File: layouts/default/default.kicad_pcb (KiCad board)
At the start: 2 copper layers, 39 x 17 mm, 21 parts

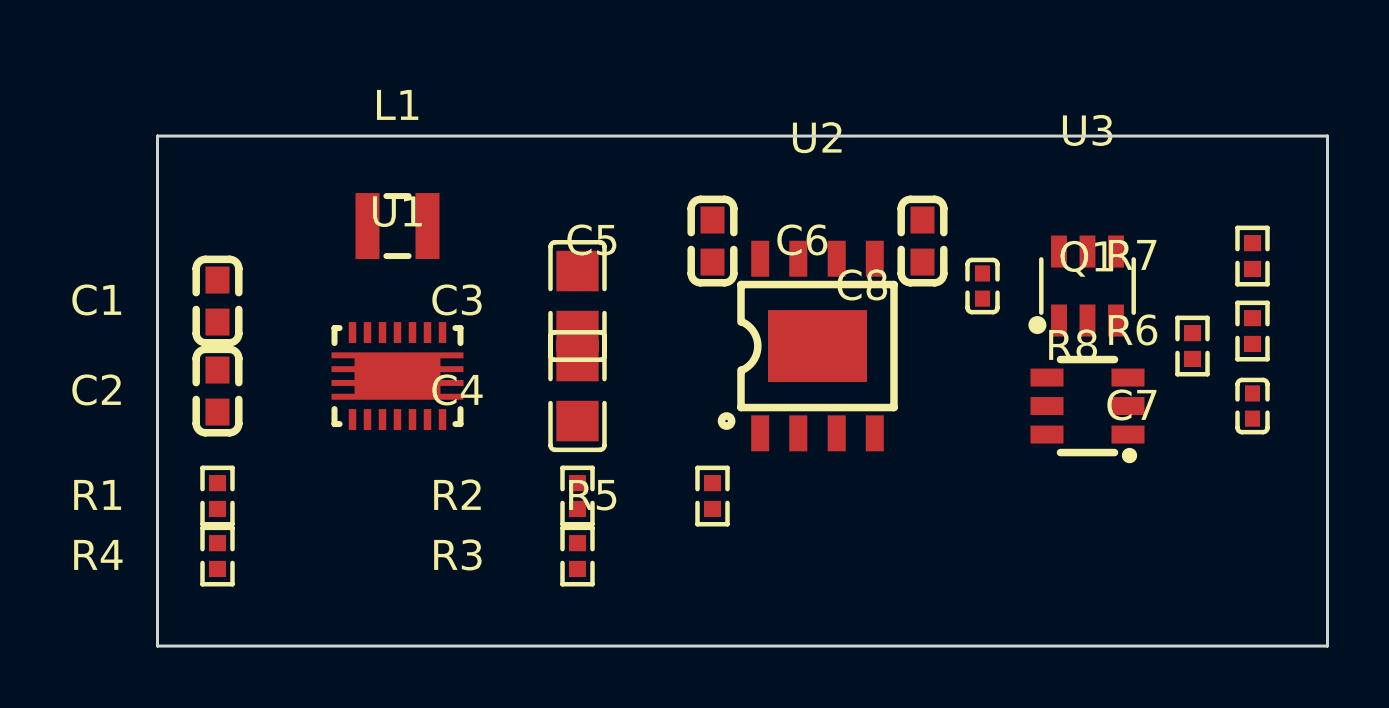
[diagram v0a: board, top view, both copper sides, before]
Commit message: Simplify: remove battery protection, add AO3401A P-MOSFET power switch for Pi (35x15mm, 19 components)
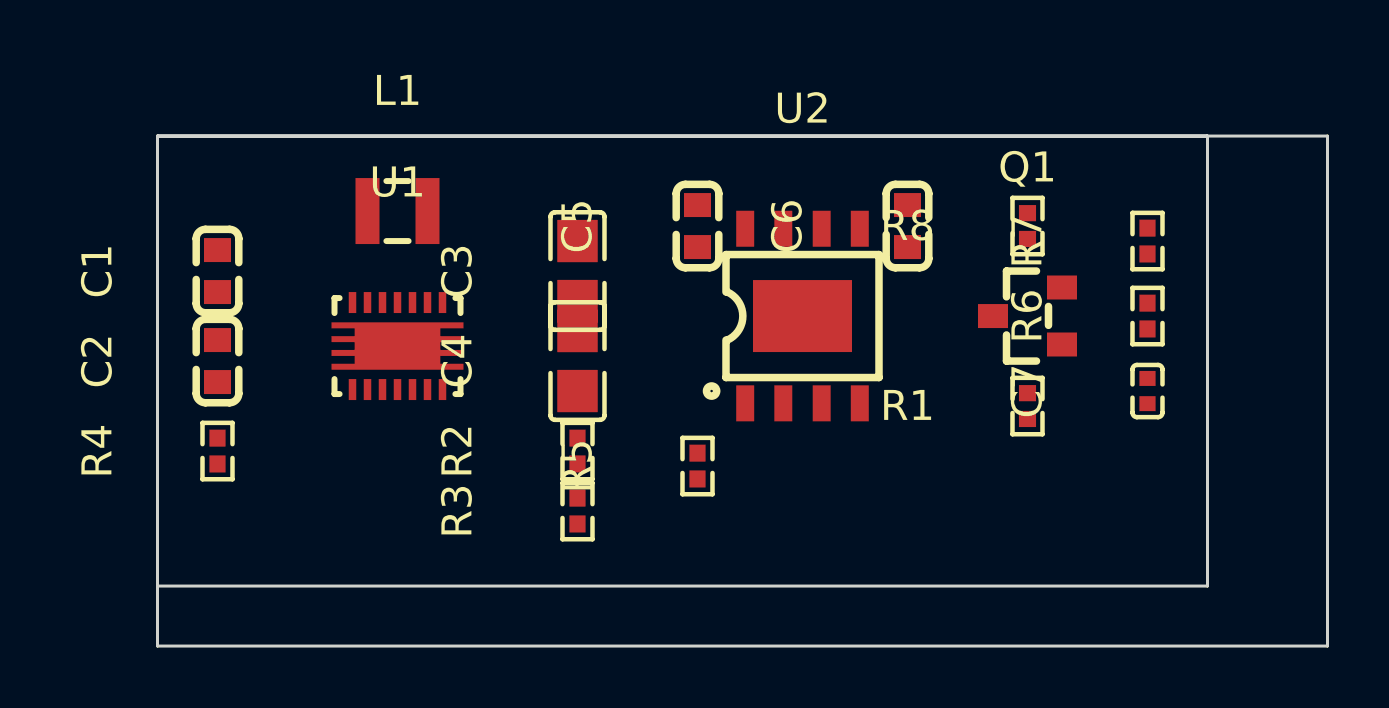
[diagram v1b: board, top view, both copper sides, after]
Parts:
- removed C8: 0F, Samsung_Electro_Mechanics_CL05B104KO5NNNC:C0402
- removed U3: , PUOLOP_DW01A:SOT-23-6_L2.9-W1.6-P0.95-LS2.8-BL
- Q1: footprint Fortune_Semicon_FS8205:SOT-23-6_L2.9-W1.6-P0.95-LS2.8-BR -> Alpha___Omega_Semicon_AO3401A:SOT-23_L2.9-W1.3-P1.90-LS2.4-BR
- R1: value 100000Ω -> 10000Ω; footprint UNI_ROYAL_0402WGF1003TCE:R0402 -> UNI_ROYAL_0402WGF1002TCE:R0402
- R8: value 100Ω -> 100000Ω; footprint UNI_ROYAL_0402WGF1000TCE:R0402 -> UNI_ROYAL_0402WGF1003TCE:R0402
- moved R1 27.2 mm to (128.0, 89.0)
- moved R8 6.80 mm to (128.0, 83.0)
- moved Q1 3.61 mm to (128.0, 86.0)
- moved C7 3.54 mm to (132.0, 88.5)
- moved R6 3.54 mm to (132.0, 86.0)
- moved R7 3.54 mm to (132.0, 83.5)
- moved R4 3.50 mm to (101.0, 90.5)
- moved R2 1.50 mm to (113.0, 90.5)
- moved R3 1.50 mm to (113.0, 92.5)
- moved R5 1.12 mm to (117.0, 91.0)
- moved U2 1.12 mm to (120.5, 86.0)
- moved C1 1.00 mm to (101.0, 84.5)
- moved C2 1.00 mm to (101.0, 87.5)
- moved C3 1.00 mm to (113.0, 84.5)
- moved C4 1.00 mm to (113.0, 87.5)
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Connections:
- C1 pad 2: c_vout2-power-lv -> lv
- C2 pad 2: c_vout2-power-lv -> lv
- C3 pad 2: c_vout2-power-lv -> lv
- C4 pad 2: c_vout2-power-lv -> lv
- C5 pad 1: hv -> c_bat-power-hv
- C5 pad 2: c_vout2-power-lv -> lv
- C6 pad 2: c_vout2-power-lv -> lv
- C7 pad 2: c_vout2-power-lv -> lv
- Q1 pad 1: c_vout2-power-lv -> pi_en
- Q1 pad 2: 2 -> c_bat-power-hv
- Q1 pad 3: lv -> hv
- R1 pad 2: c_vout2-power-lv -> lv
- R2 pad 2: c_vout2-power-lv -> lv
- R4 pad 2: c_vout2-power-lv -> lv
- R5 pad 2: c_vout2-power-lv -> lv
- R6 pad 2: c_vout2-power-lv -> lv
- R7 pad 1: hv -> c_bat-power-hv
- R8 pad 1: lv -> c_bat-power-hv
- R8 pad 2: VM -> pi_en
- U1 pad 12: pi_en -> hv
- U1 pad 15: c_vout2-power-lv -> lv
- U1 pad 2: c_vout2-power-lv -> lv
- U2 pad 1: c_vout2-power-lv -> lv
- U2 pad 3: c_vout2-power-lv -> lv
- U2 pad 5: hv -> c_bat-power-hv
- U2 pad 9: c_vout2-power-lv -> lv
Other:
- outline, holes or cut-outs redrawn

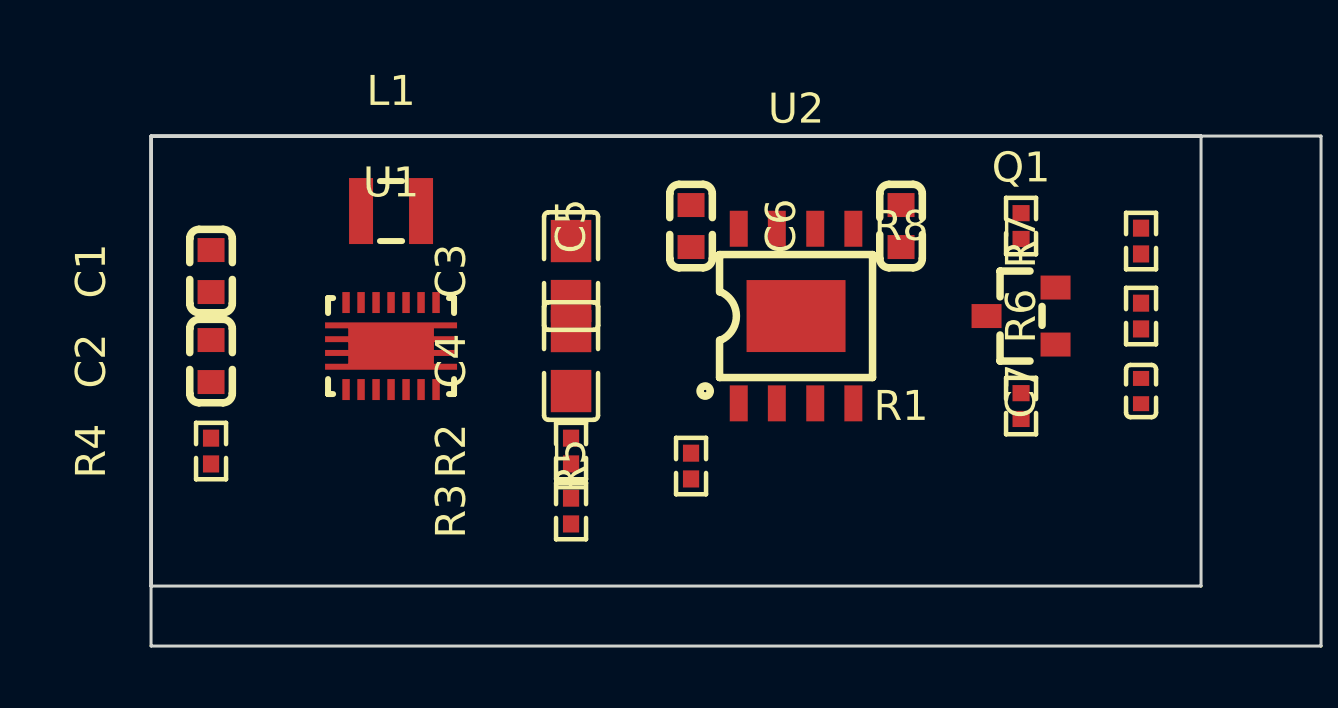
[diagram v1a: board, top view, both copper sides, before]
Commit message: Remove battery monitor (mainboard handles it), 16 components on 32x15mm
Firmware confirmed: zardam's rpi.h uses PB9 P-channel MOSFET
- PowerPin(GPIOB, 9), drive low = on, float = off
- Matches our AO3401A + 100k pull-up circuit exactly
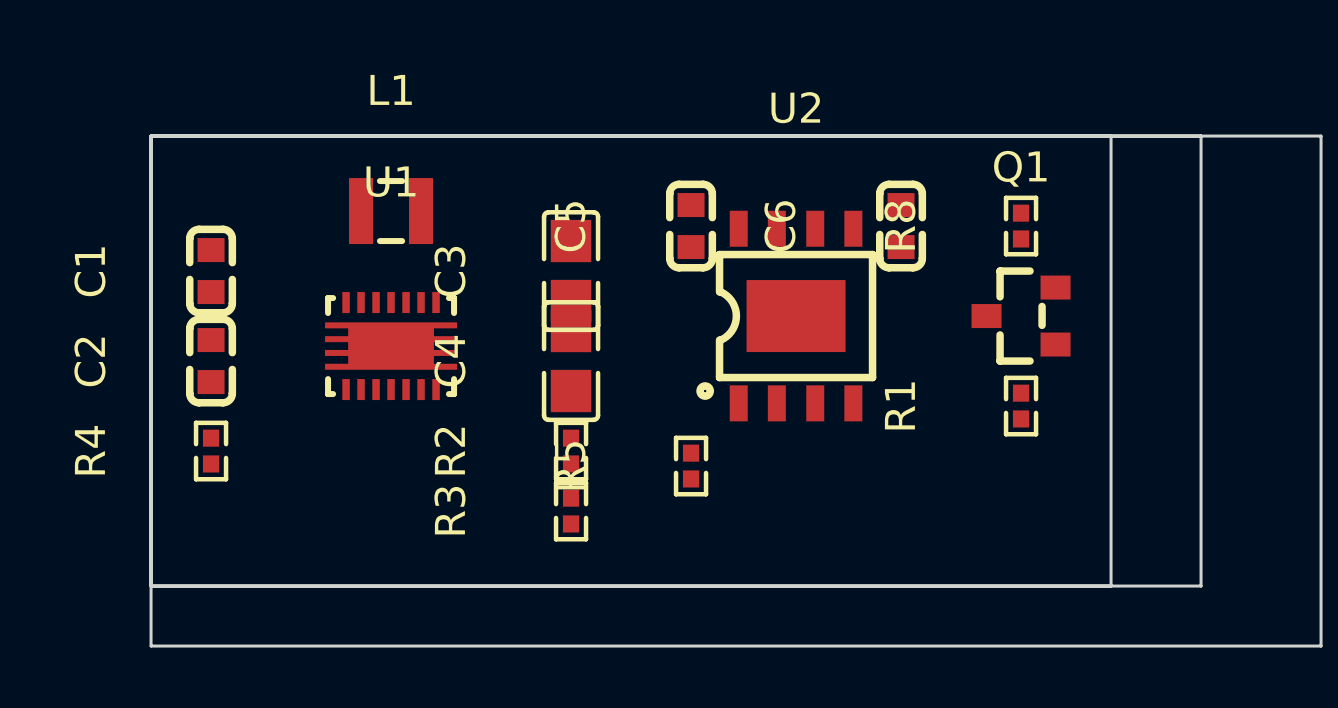
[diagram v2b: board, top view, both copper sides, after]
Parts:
- removed C7: 0F, Samsung_Electro_Mechanics_CL05B104KO5NNNC:C0402
- removed R6, R7: 1000000Ω, UNI_ROYAL_0402WGF1004TCE:R0402
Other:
- outline, holes or cut-outs redrawn

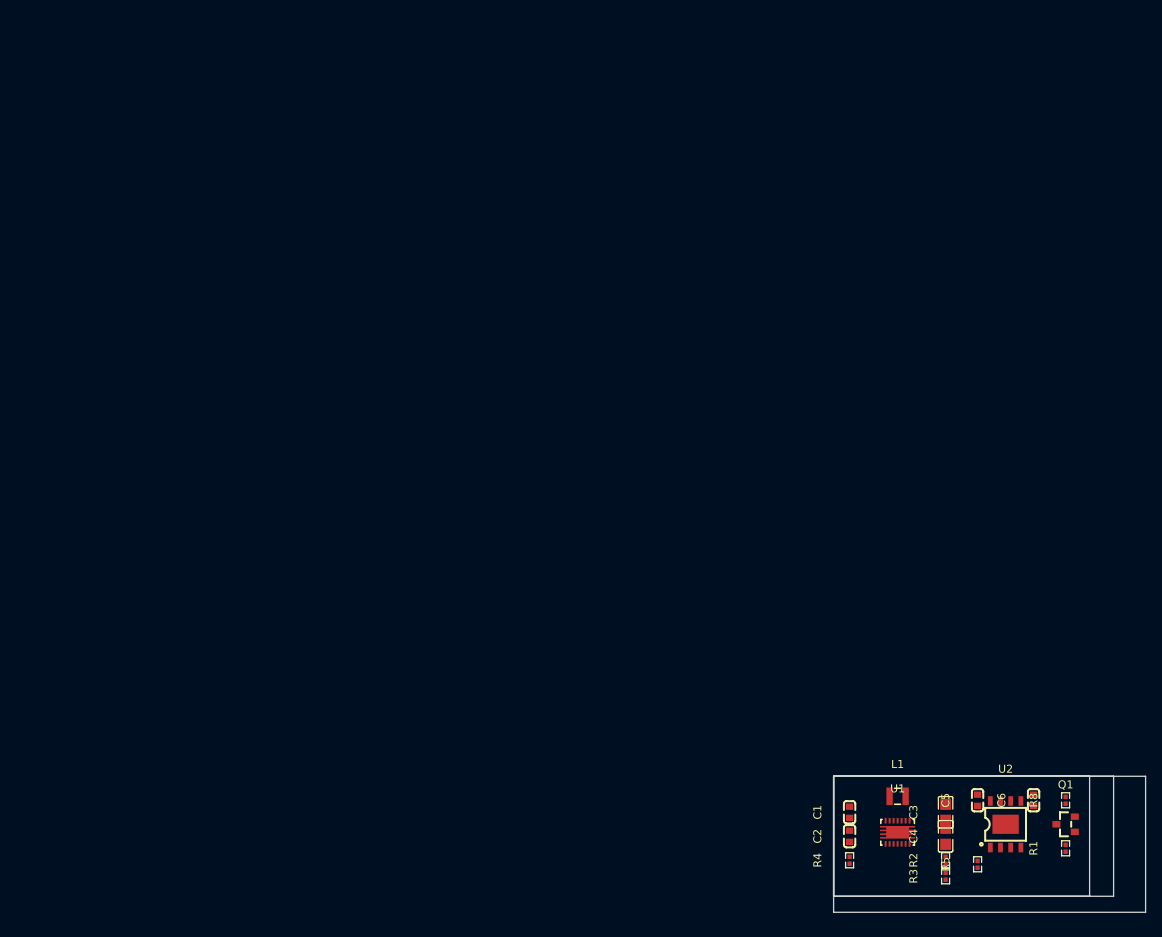
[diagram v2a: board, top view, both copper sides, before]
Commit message: Replace TPS63020 with SX1308 boost converter
- SX1308 (C78162): SOT-23-6, 2A output, hand-solderable
- Added SS34 Schottky diode (C8678) for async boost rectification
- Simplified MOSFET gate: removed unnecessary R_gate to GND, keep only 100kΩ pull-up
- Removed TPS63020 (VSON-14 pads too small for hand soldering)
- Feedback divider: 220kΩ/30kΩ → 5.0V output
- BOM reduced from 16 to 12 components
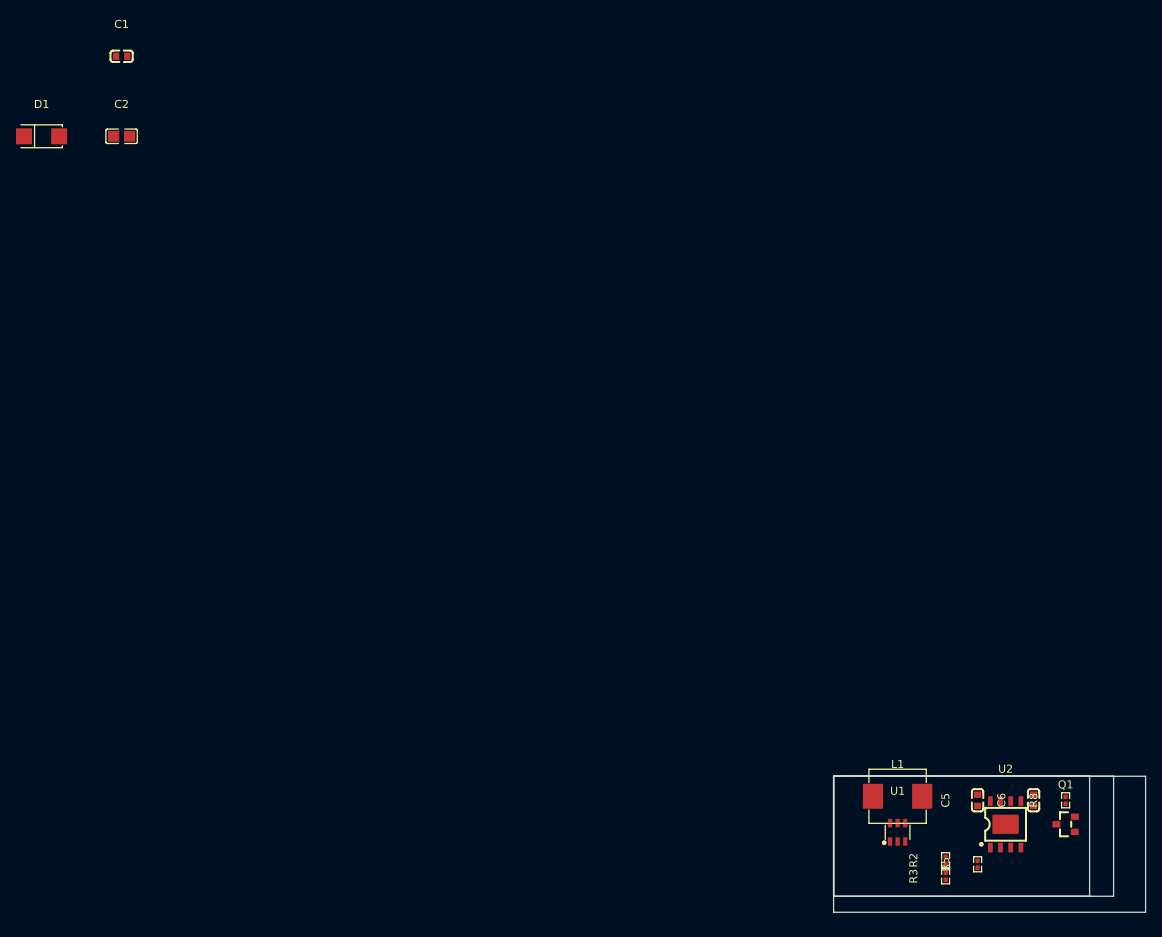
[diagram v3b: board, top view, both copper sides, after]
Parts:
- removed C3, C4: 0F, Samsung_Electro_Mechanics_CL21A226MAQNNNE:C0805
- removed R1: 10000Ω, UNI_ROYAL_0402WGF1002TCE:R0402
- removed R4: 100000Ω, UNI_ROYAL_0402WGF1003TCE:R0402
- added D1: , MDD_Microdiode_Electronics_SS34:SMA_L4.3-W2.6-LS5.2-RD, F.Cu at (0.00, 0.00)
- C2: footprint Samsung_Electro_Mechanics_CL10A106KP8NNNC:C0603 -> Samsung_Electro_Mechanics_CL21A226MAQNNNE:C0805
- L1: footprint cjiang_FTC252012S2R2MBCA:IND-SMD_L2.5-W2.0_MHCHL2520 -> SXN_SMMS0630_220M:IND-SMD_L7.3-W6.6_MHCI06030
- R2: value 110000Ω -> 30000Ω; footprint FOJAN_FRC0402F1103TS:R0402 -> UNI_ROYAL_0402WGF3002TCE:R0402
- R3: value 1000000Ω -> 220000Ω; footprint UNI_ROYAL_0402WGF1004TCE:R0402 -> UNI_ROYAL_0402WGF2203TCE:R0402
- U1: footprint Texas_Instruments_TPS63020DSJR:VSON-14_L4.0-W3.0-P0.50-BL-EP_TI_DSJ -> SX_SX1308:SOT-23-6_L2.9-W1.6-P0.95-LS2.8-BL
- moved C1 131.2 mm to (10.0, -10.0), turned to 0 degrees
- moved C2 126.2 mm to (10.0, 0.00), turned to 0 degrees
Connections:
- C2 pad 1: hv -> c_out-power-hv
- L1 pad 1: 8 -> hv
- L1 pad 2: 6 -> A
- R3 pad 1: c_vout2-power-hv -> c_out-power-hv
- U1 pad 1: hv -> (no net)
- U1 pad 2: lv -> (no net)
- U1 pad 3: FB -> (no net)
- U1 pad 4: c_vout2-power-hv -> (no net)
- U1 pad 5: c_vout2-power-hv -> (no net)
- U1 pad 6: 6 -> (no net)

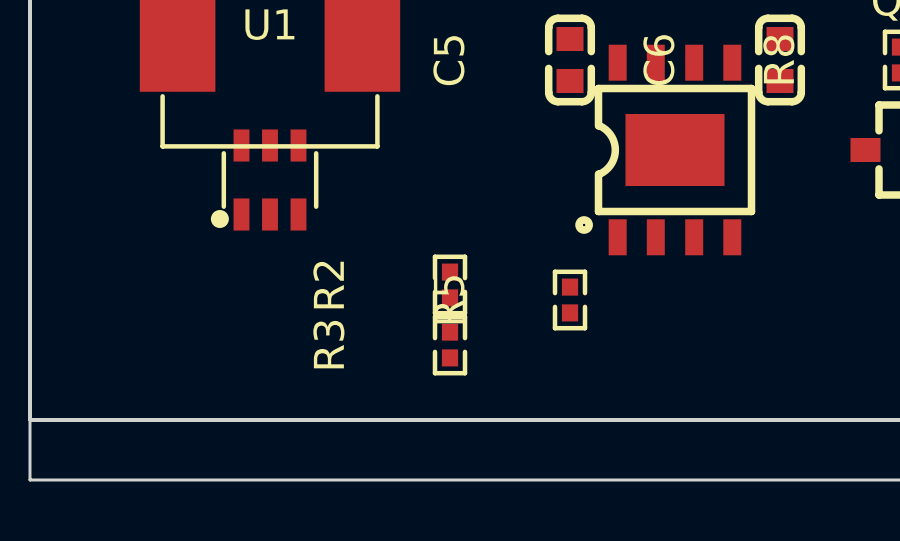
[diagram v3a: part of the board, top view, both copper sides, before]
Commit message: Optimize JLCPCB cost: use 0603 feedback resistors (Basic parts)
30kΩ and 220kΩ are Extended in 0402 but Basic in 0603.
Saves $6 in extended part fees (from $15 to $9).
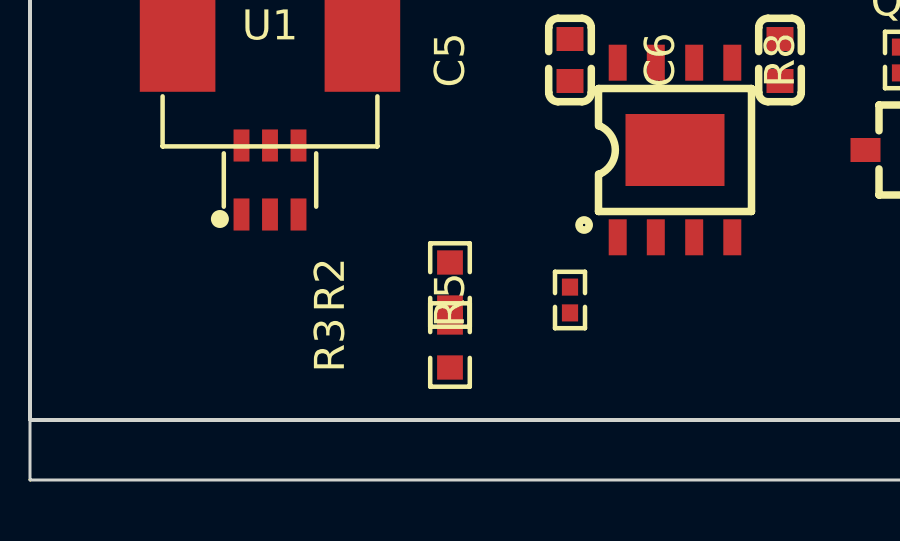
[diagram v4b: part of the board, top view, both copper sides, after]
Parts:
- R2: footprint UNI_ROYAL_0402WGF3002TCE:R0402 -> UNI_ROYAL_0603WAF3002T5E:R0603
- R3: footprint UNI_ROYAL_0402WGF2203TCE:R0402 -> UNI_ROYAL_0603WAF2203T5E:R0603
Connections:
- U1 pad 1: (no net) -> A
- U1 pad 2: (no net) -> lv
- U1 pad 3: (no net) -> FB
- U1 pad 4: (no net) -> hv
- U1 pad 5: (no net) -> hv
